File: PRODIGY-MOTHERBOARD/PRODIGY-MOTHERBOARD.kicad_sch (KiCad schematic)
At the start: 0 parts

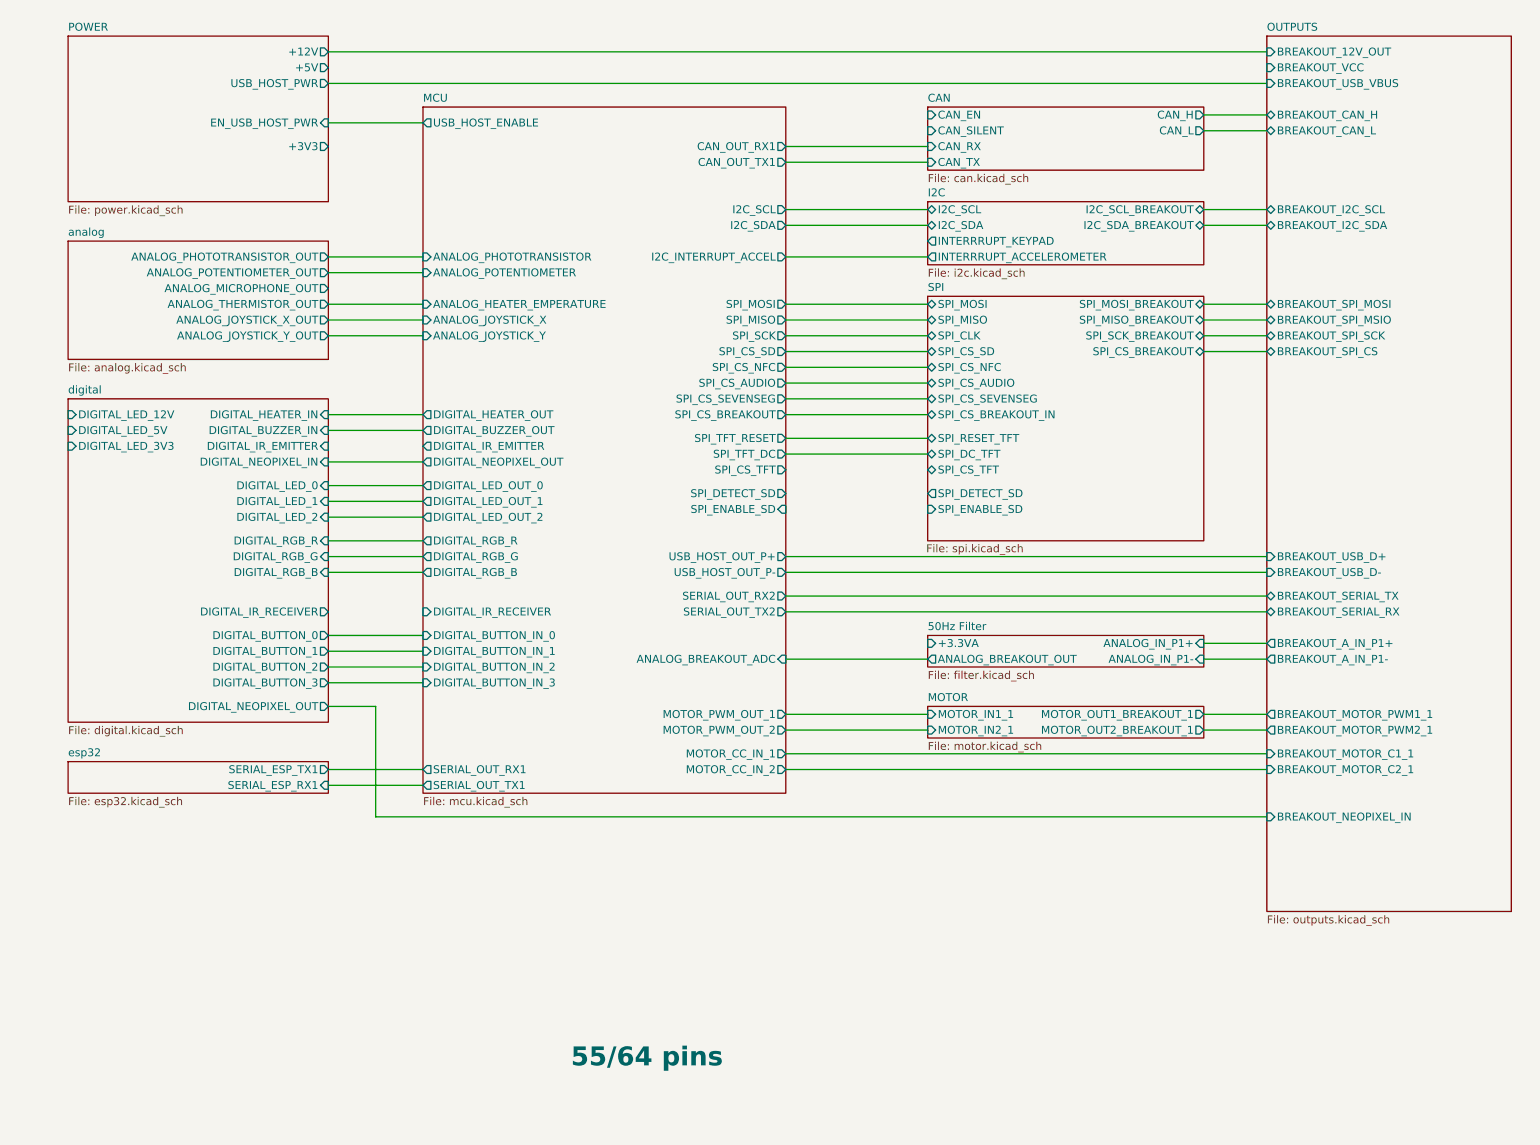
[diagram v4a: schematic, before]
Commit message: Submitted V0 for evaluation. Avaiting feedback.
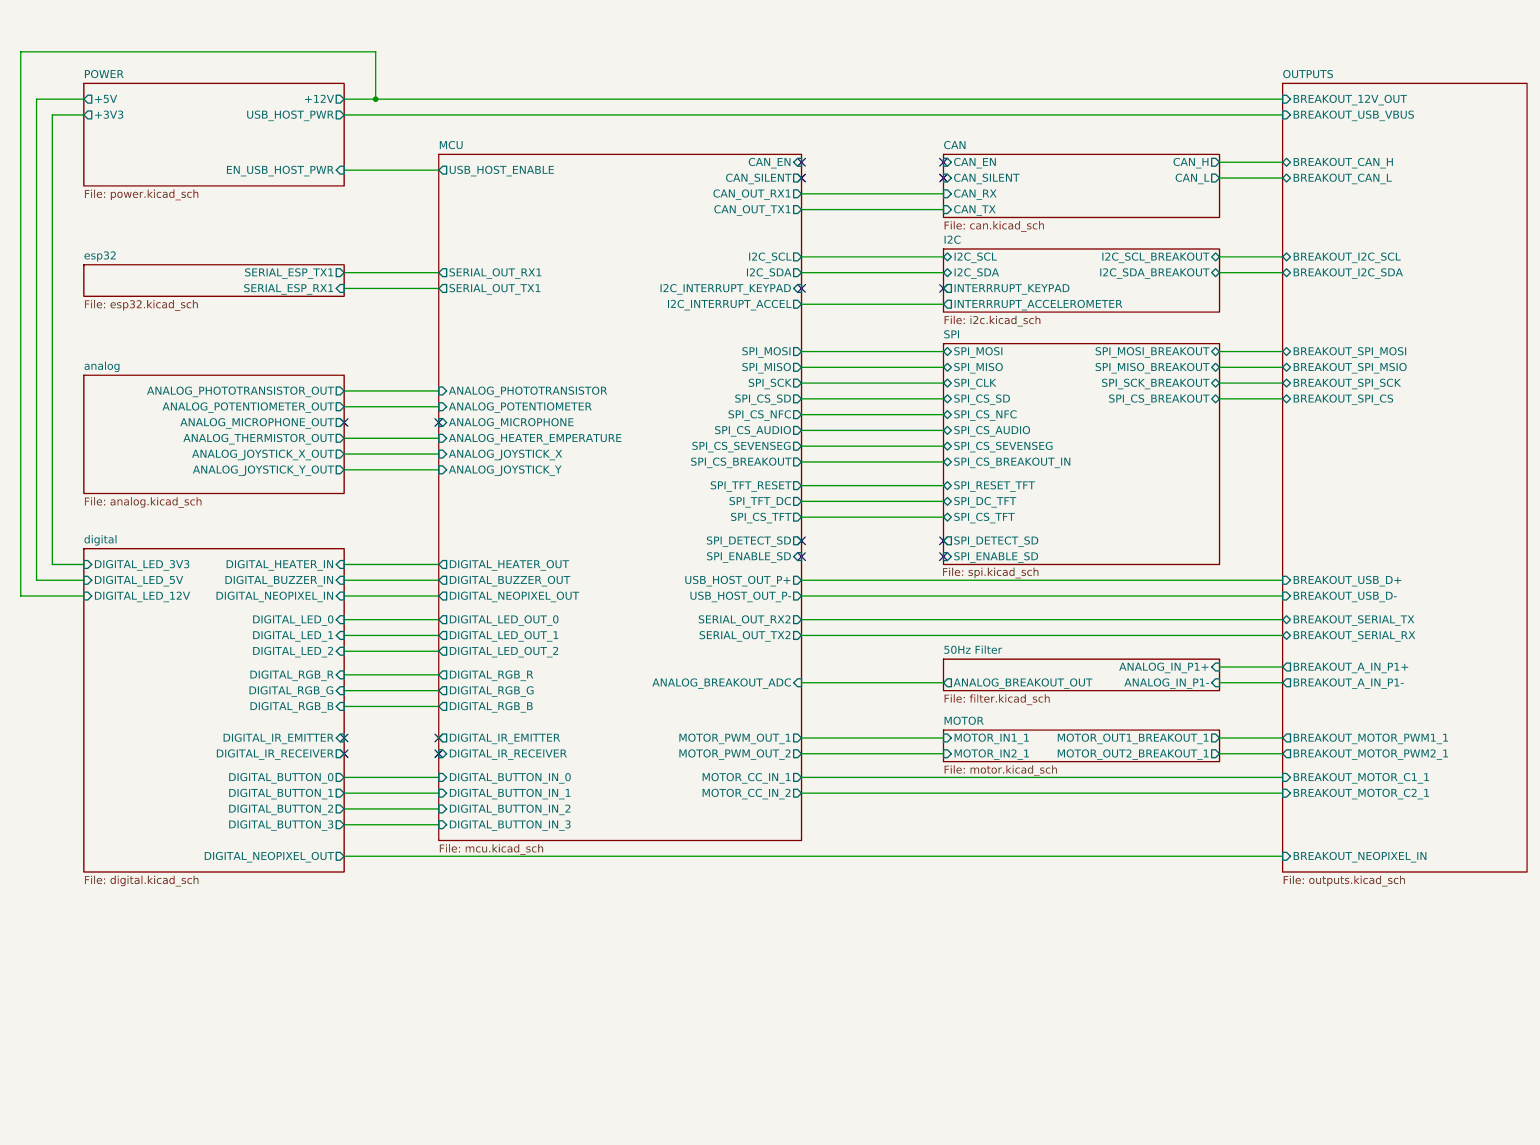
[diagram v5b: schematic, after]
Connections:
- no-connect marks 0 -> 16
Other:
- sheet 50Hz Filter ports: added none; removed +3.3VA
- sheet MCU ports: added ANALOG_MICROPHONE, CAN_EN, CAN_SILENT, I2C_INTERRUPT_KEYPAD; removed none
- sheet OUTPUTS ports: added none; removed BREAKOUT_VCC
- note removed: "55/64 pins"

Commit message: MCU schematic done. Started Analog design.
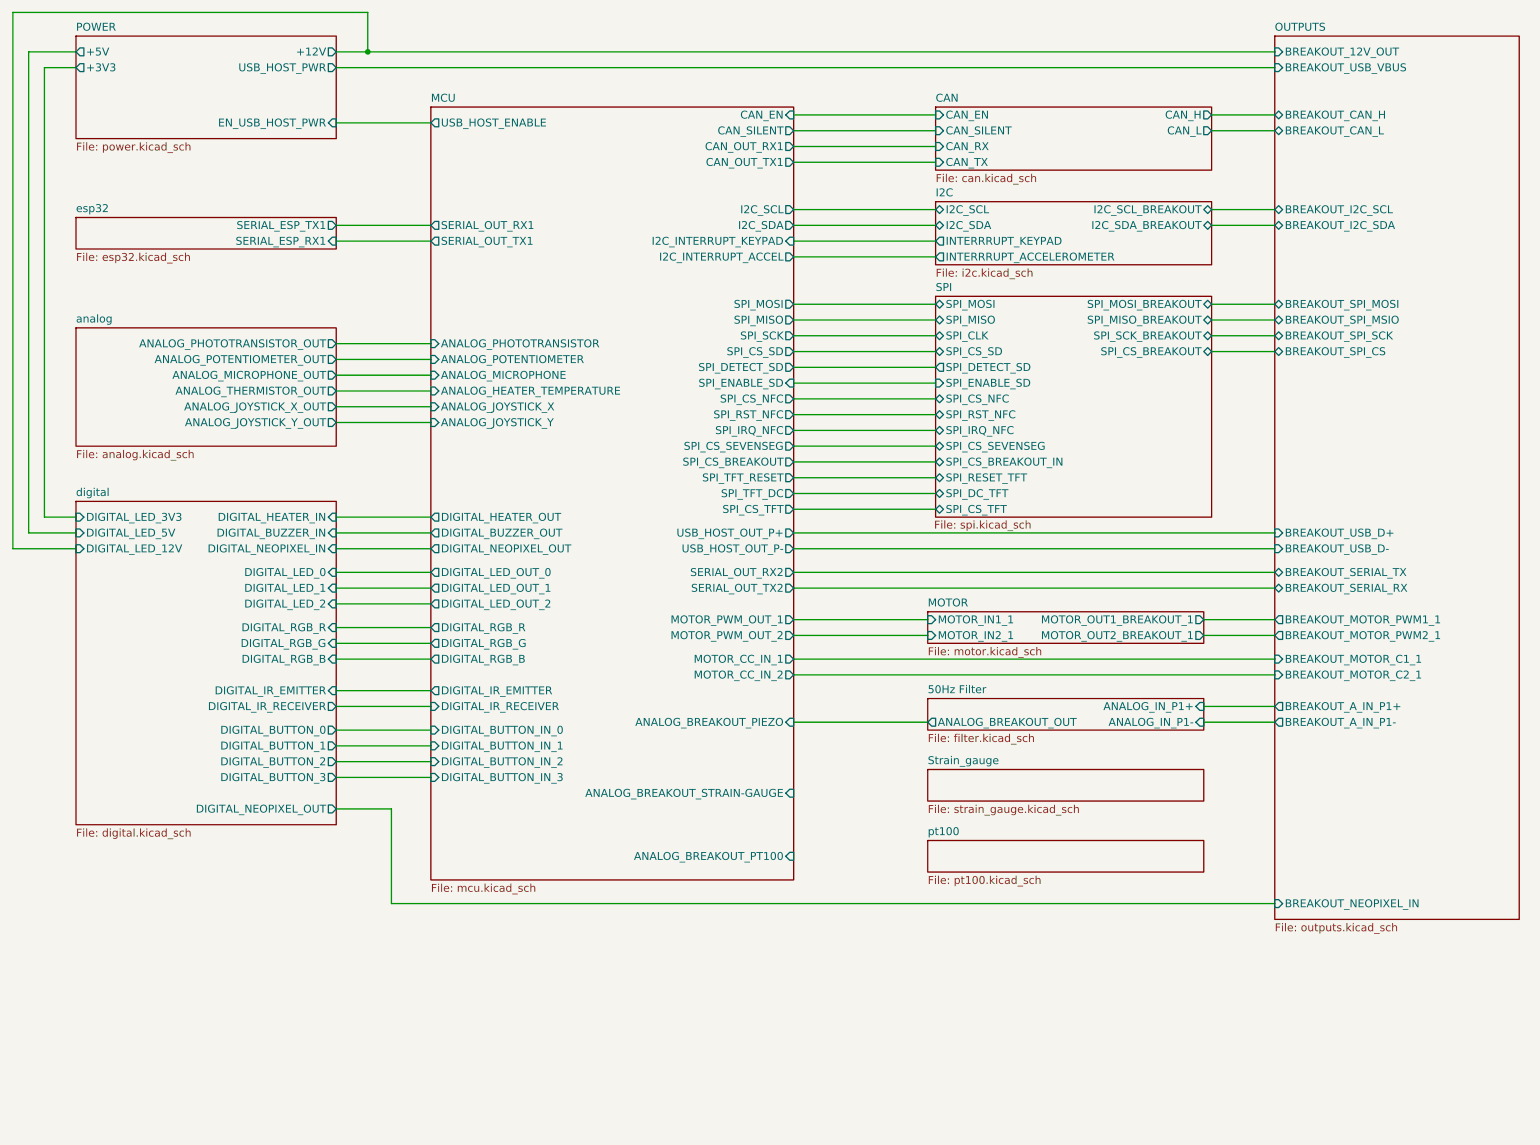
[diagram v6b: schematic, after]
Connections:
- no-connect marks 16 -> 0
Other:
- added sheet Strain_gauge (strain_gauge.kicad_sch)
- added sheet pt100 (pt100.kicad_sch)
- sheet MCU ports: added ANALOG_BREAKOUT_PIEZO, ANALOG_BREAKOUT_PT100, ANALOG_BREAKOUT_STRAIN-GAUGE, ANALOG_HEATER_TEMPERATURE, SPI_IRQ_NFC, SPI_RST_NFC; removed ANALOG_BREAKOUT_ADC, ANALOG_HEATER_EMPERATURE, SPI_CS_AUDIO
- sheet SPI ports: added SPI_IRQ_NFC, SPI_RST_NFC; removed SPI_CS_AUDIO

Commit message: Finished v0.1 schematic.
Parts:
- added FID1, FID2, FID3, FID4, FID5, FID6: Fiducial, symbol Mechanical:Fiducial
- added H1, H2, H3, H4: MountingHole, MountingHole:MountingHole_3.2mm_M3_ISO7380_Pad_TopBottom, symbol Mechanical:MountingHole
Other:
- removed sheet Strain_gauge
- sheet MCU ports: added none; removed ANALOG_BREAKOUT_STRAIN-GAUGE
- sheet OUTPUTS ports: added RTD_W1, RTD_W2, RTD_W3, RTD_W4; removed none
- sheet pt100 ports: added RTD_A_OUT, RTD_W1, RTD_W2, RTD_W3, RTD_W4; removed none

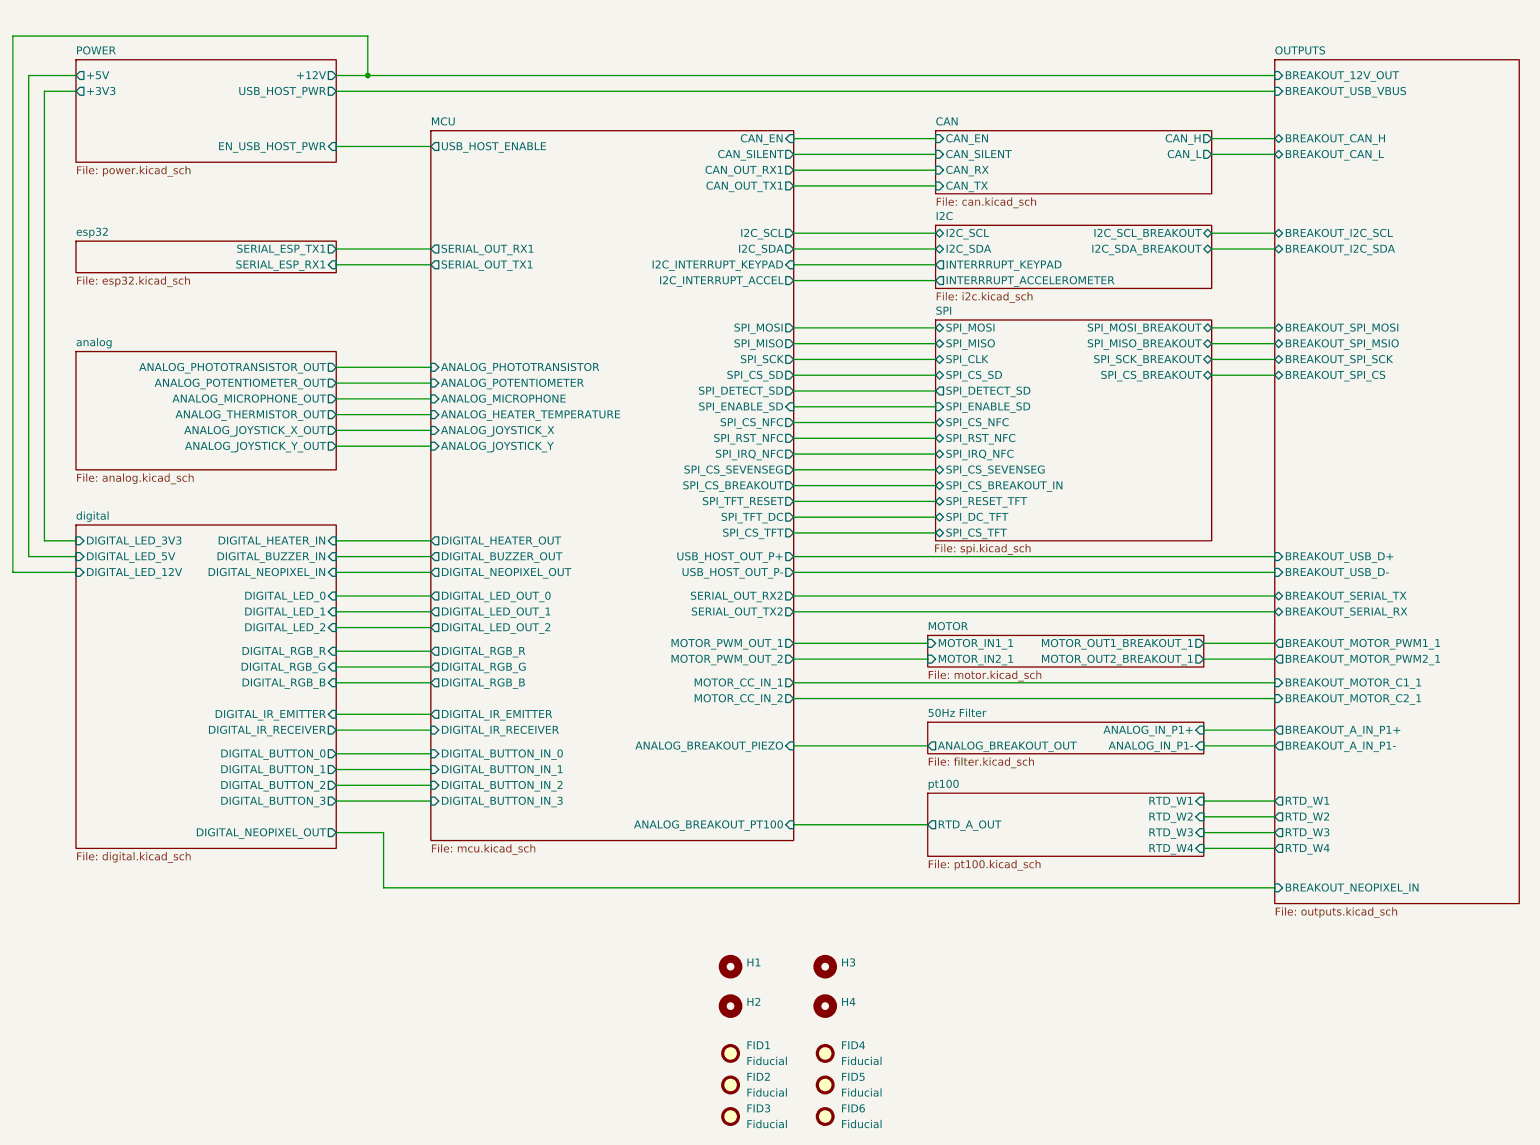
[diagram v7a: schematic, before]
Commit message: MBT Schematic improved
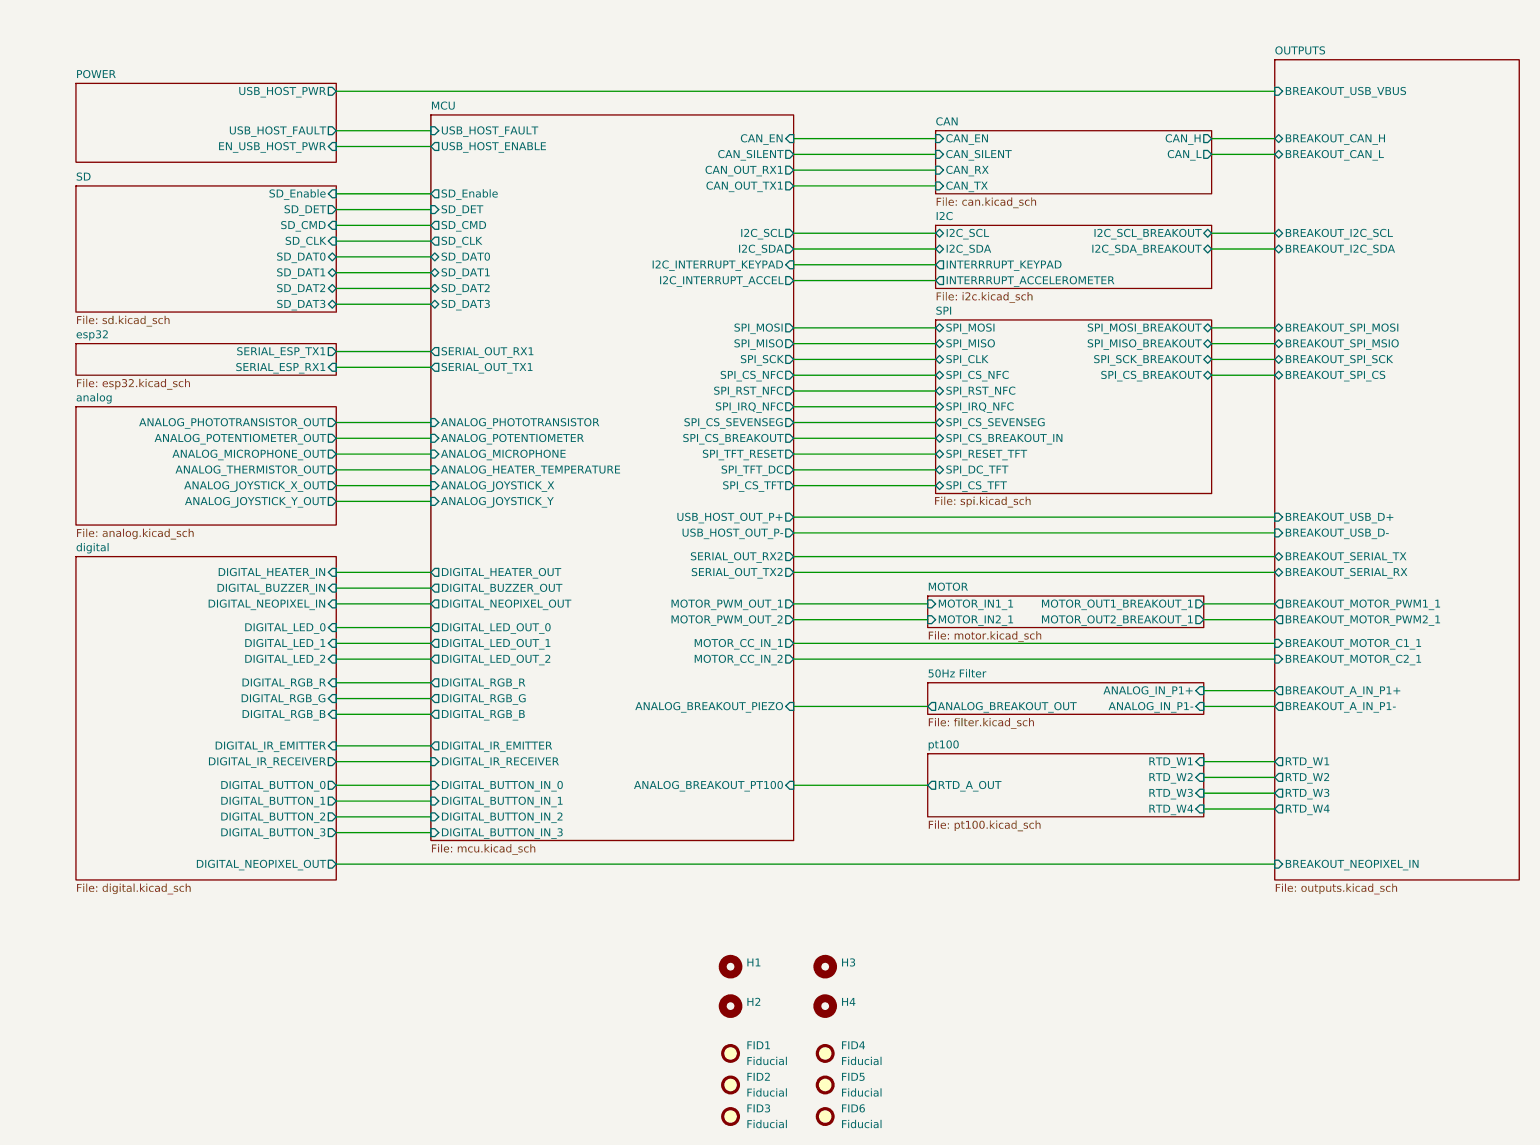
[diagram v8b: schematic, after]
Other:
- added sheet SD (sd.kicad_sch)
- sheet MCU ports: added SD_CLK, SD_CMD, SD_DAT0, SD_DAT1, SD_DAT2, SD_DAT3, SD_DET, SD_Enable, USB_HOST_FAULT; removed SPI_CS_SD, SPI_DETECT_SD, SPI_ENABLE_SD
- sheet OUTPUTS ports: added none; removed BREAKOUT_12V_OUT
- sheet POWER ports: added USB_HOST_FAULT; removed +12V, +3V3, +5V
- sheet SPI ports: added none; removed SPI_CS_SD, SPI_DETECT_SD, SPI_ENABLE_SD
- sheet digital ports: added none; removed DIGITAL_LED_12V, DIGITAL_LED_3V3, DIGITAL_LED_5V
